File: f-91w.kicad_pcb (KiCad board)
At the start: 4 copper layers, 24.4 x 24.4 mm, 46 parts, among them P1 CONN_01X01, P10 CONN_01X01, P11 CONN_01X01, P13 CONN_01X01, P14 CONN_01X01, P2 CONN_01X01, P3 CONN_01X01, P5 CONN_01X01, P6 CONN_01X01, P7 CONN_01X01, P8 CONN_01X01, P9 CONN_01X01, Q1 BC846, U1 CY8C4248LQI-BL483, U2 LCD-F-91W, U3 BME680, Y1 32.768KHz, Y2 24MHz

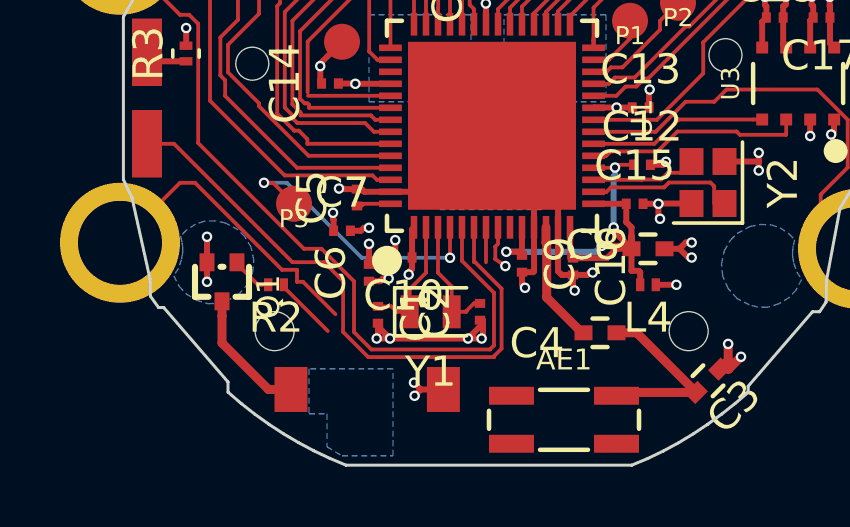
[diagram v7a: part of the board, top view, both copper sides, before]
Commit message: Reconnected traces broken by antenna placement
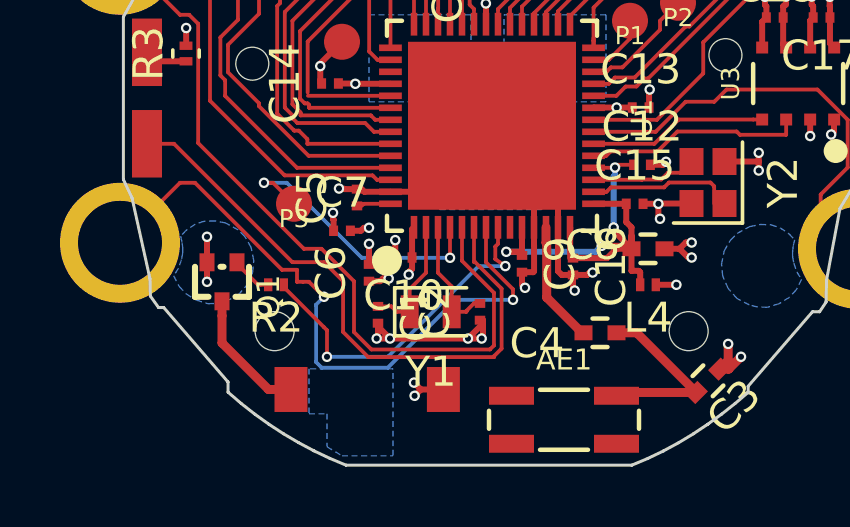
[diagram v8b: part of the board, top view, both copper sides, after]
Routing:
- net /B_MODE: track 11.2 -> 22.1 mm, vias 0 -> 2
- net /BUZ_EN: track 3.75 -> 11.8 mm, vias 1 -> 2
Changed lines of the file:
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@@
     (thickness 0.6)
     (drawings 508)
-    (tracks 503)
+    (tracks 520)
     (zones 0)
     (modules 46)
@@
   (segment (start 47.8055 95.851) (end 46.801 95.851) (width 0.2) (layer F.Cu) (net 32))
   (segment (start 46.801 95.851) (end 46.5 95.55) (width 0.2) (layer F.Cu) (net 32))
+  (segment (start 57.4 102.542267) (end 57.434499 102.542267) (width 0.127) (layer F.Cu) (net 33))
+  (segment (start 57.434499 102.542267) (end 58.319511 103.427279) (width 0.127) (layer F.Cu) (net 33))
   (segment (start 57.4 101.385) (end 57.4 102.542267) (width 0.127) (layer F.Cu) (net 33))
   (segment (start 47.4 98.6) (end 46.5 98.6) (width 0.127) (layer F.Cu) (net 33))
   (segment (start 58.319511 105.427155) (end 58.070654 105.676012) (width 0.127) (layer F.Cu) (net 33))
   (segment (start 51.34599 102.54599) (end 47.4 98.6) (width 0.127) (layer F.Cu) (net 33))
-  (segment (start 57.4 102.542267) (end 57.434499 102.542267) (width 0.127) (layer F.Cu) (net 33))
-  (segment (start 57.434499 102.542267) (end 58.319511 103.427279) (width 0.127) (layer F.Cu) (net 33))
   (segment (start 58.319511 103.427279) (end 58.319511 105.427155) (width 0.127) (layer F.Cu) (net 33))
   (segment (start 58.070654 105.676012) (end 58.070654 105.710511) (width 0.127) (layer F.Cu) (net 33))
@@
   (segment (start 61.955498 98.854013) (end 61.809511 99) (width 0.127) (layer F.Cu) (net 36))
   (segment (start 61.809511 99) (end 61.385 99) (width 0.127) (layer F.Cu) (net 36))
+  (segment (start 57 101.385) (end 57 102.501491) (width 0.127) (layer F.Cu) (net 37))
   (segment (start 51.730058 102.1) (end 48.205501 98.575443) (width 0.127) (layer F.Cu) (net 37))
-  (segment (start 57 101.385) (end 57 102.501491) (width 0.127) (layer F.Cu) (net 37))
   (segment (start 58.065501 105.321941) (end 57.930941 105.456501) (width 0.127) (layer F.Cu) (net 37))
   (segment (start 57 102.501491) (end 58.065501 103.566992) (width 0.127) (layer F.Cu) (net 37))
@@
   (segment (start 48.205501 98.575443) (end 48.205501 94.600059) (width 0.127) (layer F.Cu) (net 37))
   (segment (start 47.599999 94.299999) (end 45.6 92.3) (width 0.127) (layer F.Cu) (net 37))
+  (segment (start 58.7 103.8) (end 58.7 103.448544) (width 0.127) (layer F.Cu) (net 38))
+  (segment (start 58.7 103.448544) (end 57.8 102.548544) (width 0.127) (layer F.Cu) (net 38))
+  (via (at 58.7 103.8) (size 0.35) (drill 0.2) (layers F.Cu B.Cu) (net 38))
+  (segment (start 56.791166 103.8) (end 58.7 103.8) (width 0.127) (layer B.Cu) (net 38))
+  (segment (start 52.4 103.7) (end 52.134499 103.965501) (width 0.127) (layer B.Cu) (net 38))
+  (segment (start 52.134499 103.965501) (end 52.134499 105.875441) (width 0.127) (layer B.Cu) (net 38))
+  (segment (start 52.134499 105.875441) (end 52.324559 106.065501) (width 0.127) (layer B.Cu) (net 38))
+  (segment (start 52.324559 106.065501) (end 54.525665 106.065501) (width 0.127) (layer B.Cu) (net 38))
+  (segment (start 54.525665 106.065501) (end 56.791166 103.8) (width 0.127) (layer B.Cu) (net 38))
+  (via (at 52.4 103.7) (size 0.35) (drill 0.2) (layers F.Cu B.Cu) (net 38))
+  (segment (start 51.9 103.2) (end 52.4 103.7) (width 0.127) (layer F.Cu) (net 38))
+  (segment (start 51.7 103.2) (end 51.9 103.2) (width 0.127) (layer F.Cu) (net 38))
   (segment (start 51 102.8) (end 51.5 102.8) (width 0.127) (layer F.Cu) (net 38))
   (segment (start 51.7 103.2) (end 51.5 103.2) (width 0.127) (layer F.Cu) (net 38))
@@
   (segment (start 47.599999 99.900001) (end 45.6 101.9) (width 0.127) (layer F.Cu) (net 38))
   (segment (start 51.5 103.2) (end 51.5 102.8) (width 0.127) (layer F.Cu) (net 38))
-  (segment (start 52.781979 104.281979) (end 51.7 103.2) (width 0.127) (layer F.Cu) (net 38))
   (segment (start 57.8 102.548544) (end 57.8 101.385) (width 0.127) (layer F.Cu) (net 38))
   (segment (start 68.9555 100.291) (end 68.9555 100.8555) (width 0.127) (layer F.Cu) (net 39))
@@
   (segment (start 63.866275 99.565501) (end 64.275499 99.565501) (width 0.127) (layer F.Cu) (net 46))
   (segment (start 64.275499 99.565501) (end 64.65 99.191) (width 0.127) (layer F.Cu) (net 46))
-  (segment (start 52.527969 104.842969) (end 51.06 103.375) (width 0.127) (layer F.Cu) (net 47))
+  (segment (start 52.4 104.715) (end 51.06 103.375) (width 0.127) (layer F.Cu) (net 47))
+  (segment (start 52.5 105.7) (end 52.5 104.815) (width 0.127) (layer F.Cu) (net 47))
+  (segment (start 52.5 104.815) (end 52.4 104.715) (width 0.127) (layer F.Cu) (net 47))
+  (via (at 52.5 105.7) (size 0.35) (drill 0.2) (layers F.Cu B.Cu) (net 47))
+  (segment (start 54.531942 105.7) (end 52.5 105.7) (width 0.127) (layer B.Cu) (net 47))
+  (segment (start 58.444333 102.675981) (end 57.555961 102.675981) (width 0.127) (layer B.Cu) (net 47))
+  (segment (start 57.555961 102.675981) (end 54.531942 105.7) (width 0.127) (layer B.Cu) (net 47))
   (segment (start 51.06 103.375) (end 51.06 103.3) (width 0.127) (layer F.Cu) (net 47))
   (segment (start 58.109999 102.445499) (end 58.444333 102.675981) (width 0.127) (layer F.Cu) (net 47))
